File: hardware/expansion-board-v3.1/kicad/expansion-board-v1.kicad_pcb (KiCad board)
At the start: 6 copper layers, 100 x 62 mm, 156 parts, among them J1 PinHeader_2x20_P2.54mm_Vertic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, J2 U.FL_Hirose_U.FL-R-SMT-1_Vert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, J4 USB_C_Receptacle_HRO_TYPE-C-3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, J5 U.FL_Hirose_U.FL-R-SMT-1_Vert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, J6 U.FL_Hirose_U.FL-R-SMT-1_Vert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, J8 U.FL_Hirose_U.FL-R-SMT-1_Vert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, Q2 SOT-23, Q3 SOT-23, Q4 SOT-23, Q5 SOT-23, SW1 SolderJumper-2_P1.3mm_Open_Pa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, SW2 SolderJumper-2_P1.3mm_Open_Pa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, U1 SOT-23-5, U10 QFN-48-1EP_7x7mm_P0.5mm_EP5.1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, U11 DFN-8-1EP_2x2mm_P0.5mm_EP0.86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, U12 SOT-363_SC-70-6, U13 AD8319_LFCSP-8-EP, U14 MSOP-8_3x3mm_P0.65mm, U15 SOT-23-6, U16 SOT-363_SC-70-6, U17 SOT-363_SC-70-6, U2 SOT-23-5, U3 SOT-23-5, U4 BNO085_LGA-28, U5 BMP388_LGA-10, U6 LGA-16_3x3mm_P0.5mm, U7 ATGM336H_LCC-18, U8 QFN-56-1EP_7x7mm_P0.4mm_EP3.2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, U9 SOIC-8_5.3x5.3mm_P1.27mm, Y1 Crystal_SMD_3225-4Pin_3.2x2.5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, Y2 Crystal_SMD_3225-4Pin_3.2x2.5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, Y3 Crystal_SMD_3215-2Pin_3.2x1.5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

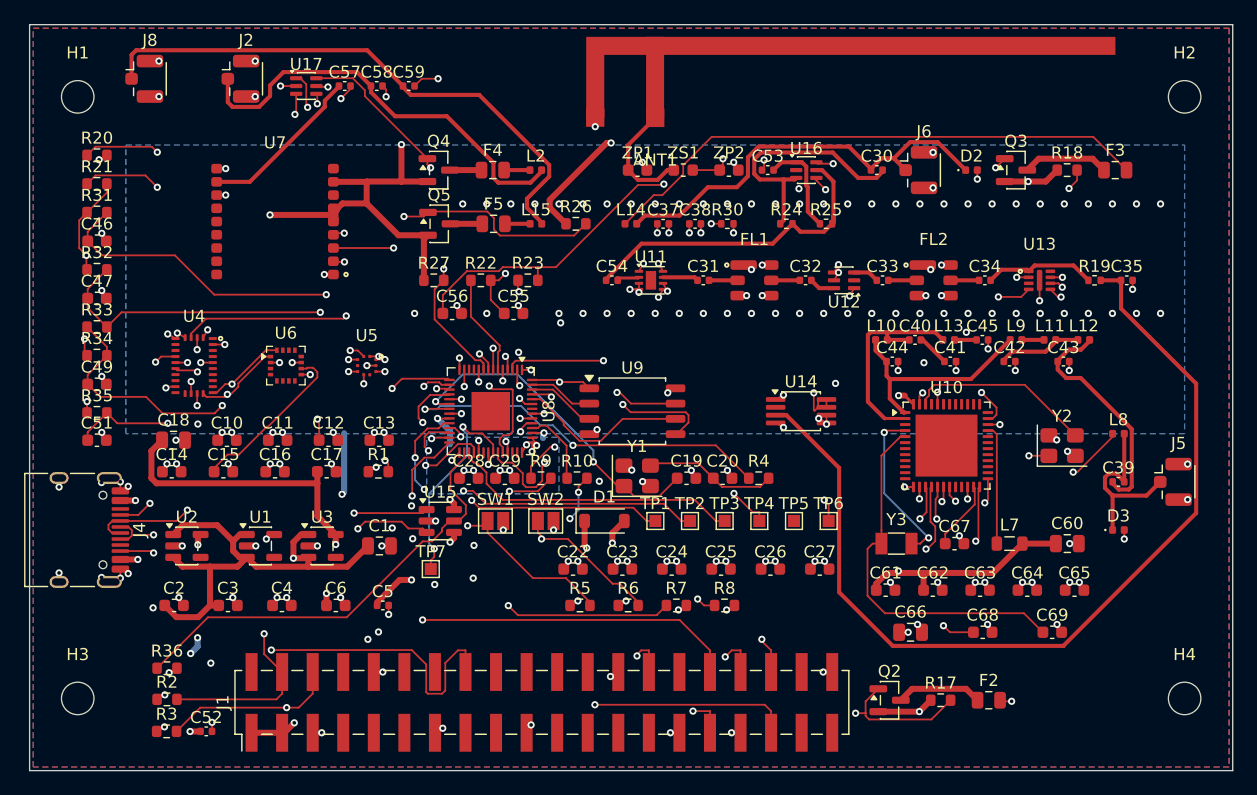
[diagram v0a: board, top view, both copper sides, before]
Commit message: feat(hw): v3.1 致命电源打通——扇出改在 route_rf 之前跑
route_rf.py 原本幂等地清掉所有 track，把 fanout_v31.py 放的扇出孔也删了。
改为只清平面网(GND/3V3_*)输出，保留信号网扇出。

新顺序：gen_pcb → fanout(空板放 9/10 孔) → route_rf(避让扇出) →
export_dsn → freerouting → import_ses。

结果：SUBG_VDDR、RP_1V1 两路致命电源打通（4层时代+上一版的死结），
板子现在能启动。铜层 DRC 0 违例。

代价：freerouting 随机性导致 RF 段 172→163（扇出挤占），5 条 RF +
USB/sub-GHz/I2C 共 15 残线待手工收尾（均非启动致命）。

下轮：RP_1V1 专用扇出（少挤 RF）+ RF 手工 F.Cu + USB/sub-GHz 手工。
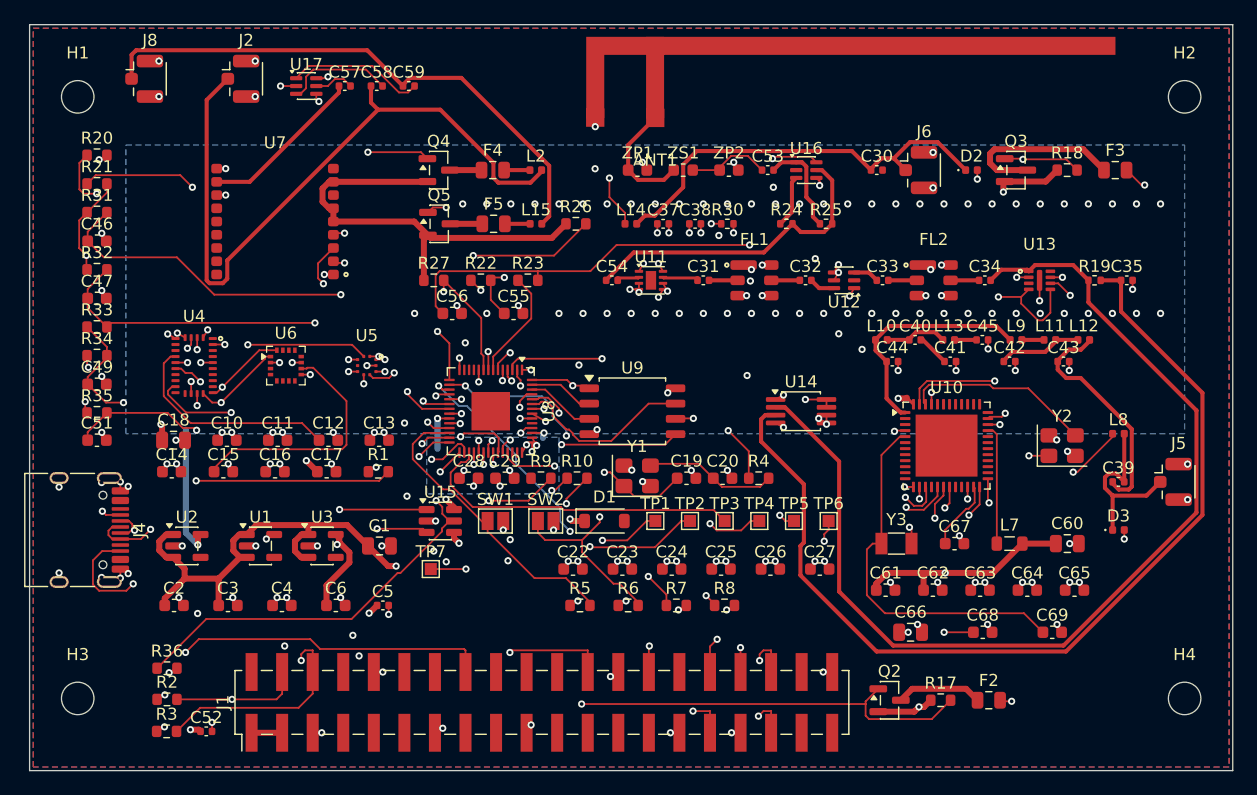
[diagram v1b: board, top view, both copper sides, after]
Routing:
- net DET_IN: track 9.26 -> 86.4 mm
- net SUBG_SCK: track 62.5 -> 0.00 mm, vias 3 -> 0
- net USB_VBUS: track 50.7 -> 0.00 mm, vias 3 -> 0
- net BARO_INT: track 0.00 -> 37.9 mm, vias 0 -> 2
- net 3V3_GNSS: track 213.3 -> 183.2 mm, vias 7 -> 6
- net DEMOD2: track 0.00 -> 28.8 mm, vias 0 -> 2
- net VCC_5V: track 85.4 -> 58.1 mm, vias 3 -> 2
- net ANT_GNSS_EXT: track 35.2 -> 58.2 mm
- net TL_PWM: track 61.8 -> 39.5 mm, vias 3 -> 2
- net SW1_J2: track 20.9 -> 4.36 mm
- net RSSI: track 63.7 -> 47.8 mm
- net SUBG_RFN: track 18.3 -> 5.20 mm
- net SUBG_TMSC: track 65.8 -> 53.2 mm, vias 3 -> 2
- net AD8313_VOUT: track 90.3 -> 78.9 mm
- net SUBG_CSN: track 59.7 -> 48.6 mm
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
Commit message: feat(hw): 收尾布线器 route_fix — 真缺线 21→10，铜层 DRC 保持 0
route_maze 布不动的真因不是复杂度，是障碍模型：它拿 track 的 bounding box
当障碍（route_maze.py:100-103），而本板 1308 段里 610 段是 45° 斜线，实测
bbox 面积 3290mm² vs 实际铜面积 778mm² —— 4.2 倍的假障碍糊满整图，A* 每次
都得翻完整个搜索空间才能报"走不通"，于是"单条几分钟"。

route_fix.py 换掉四处：
· 线段光栅化代替 bbox，代价正比线长而非包围盒面积，不再产生假障碍
· (count, owner) 双数组代替 per-net 重建占用区，查询 O(1)，一次建图全程复用
· 按网络类分档（Default 0.15/0.15、POWER 0.3/0.2、RF50 0.34/0.15）。原来
  全板按最严的 0.2 净空一刀切，比板规严得多
· 连通块解析：DRC 说的是"这两块铜没连上"，起点必须是整块铜而不是一个点

另加两个针对本板的机制：
· 焊盘逃逸 stub —— QFN 引脚该沿轴向出线，精确算 U10（0.5mm pitch）邻居边缘
  到中心线 0.375mm > 0.3 线所需的 0.35mm，是过得去的；0.15mm 栅格表达不了
  这 0.025mm 余量才误判成"几何封死"。这一段用连续几何算，绕开栅格
· 平面命中 —— In3.Cu 是 3V3_DIG 满板平面，打过孔落到填充铜上即连通，不必
  横穿半块板去够对面焊盘。判据必须是 HitTestFilledArea 而非层号，否则起点
  自己在 In3 上有段走线就会"零节点成功"

顺带修掉两个会进制造文件的真 bug：
· 过孔穿层漏检：通孔穿透全部 6 层，原先只校验起止两层，中间层直撞别人走线，
  实测放过 9 条 Via[X] on F.Cu-B.Cu <-> Track[Y] on In2/In3
· 栅格化误差：栅格只保证格点在安全圈外，45° 步长 0.212mm 的线段中点偏离
  格点 0.106mm，能蹭进净空（实测漏过 actual 0.1586 < 0.2）。现在落盘前一律
  做连续几何复核，不过就弃用该路径——宁可不布，不往板里塞违例

实测：未连通 28→17，真缺线 21→10，铜层 DRC 0→0，射频 163 段全 F.Cu、0 过孔
完全没动，整批 32 秒（原先单条几分钟）。

rip-up & reroute 也实现了（collect_blockers/strip），但结论是不该用：拆掉的线
重布不回来，迭代在 14→18→17 之间震荡且引入 20 条 clearance/shorting，已加验收
回滚。默认不启用。

⚠️ score.py 的口径偏乐观（报 3 处 vs DRC 10 处）：焊盘落在覆铜填充区就算连上，
而 KiCad 可能因 thermal spoke 不足判未连接。参考用，别当验收。

另记一条坑：check_route.py 的三分类不稳定，同一份文件跑两次会在 12/13/3 和
21/2/5 之间漂——同一个未连通对，KiCad 描述成 Pad↔X 还是 Track↔X 取决于内部
遍历顺序。验收要盯"未连通总数 + 铜层 DRC"这两个稳定量。
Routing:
- net 3V3_DIG: track 36.0 -> 68.3 mm
- net VCC_5V: track 58.1 -> 78.0 mm
- net RP_1V1: track 9.95 -> 21.3 mm, vias 5 -> 6
- net USB_VBUS: track 0.00 -> 10.5 mm, vias 0 -> 2

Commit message: fix(hw): 修掉会把短路写进板子的碰撞判定 bug；In3 锁电源平面，3V3 未连通 6→0
## 一、碰撞判定漏判交叉 —— 会真的短路，最要紧

route_fix 判两条走线冲突用的是"四端点到对方线段距离取最小"。这个公式对
**交叉**的线段返回正值：两条线真穿过彼此时，四个端点离对方线段都可能很远。

实测它布出来的 SWDIO：
    SWDIO     (104.890,91.253)→(104.890,92.353)   垂直
    SUBG_CSN  (122.332,91.980)→(103.615,91.980)   水平
    交点 (104.890,91.980) 落在两段内 —— 真短路
    公式却算出 0.3733mm、余量 +0.07mm，判为合规

seg_seg_dist 加叉积跨越判定，相交返回 0。回归：交叉→0.0，平行→1.0。
修完 route_fix 老实报"SWDIO 走不通，挡路者 SWCLK/SUBG_CSN"，不再硬布。
fanout_ring 里同样的写法一并修（它的 stub_ok 也是四端点取最小）。

KiCad DRC 本身会抓 tracks_crossing，而每次落盘都跑 DRC，所以短路没进过
制造文件——但工具带着这个 bug 就是隐患。

## 二、3V3 未连通的真因不是线宽，是叠层用途冲突

In3.Cu 既铺 3V3_DIG 电源平面（4780mm²），又被 freerouting 走了 181 段信号，
覆铜避让把平面切成 14 块孤岛，KiCad 直接报
"Zone [3V3_DIG] on In3.Cu ↔ Zone [3V3_DIG] on In3.Cu"。

· export_dsn 把 In3 加进 PLANE_LAYERS 锁死（走线层 4→3，B.Cu 原本只用了
  24 段，余量足够吸收被赶出来的 181 段）
· route_fix 的 A* 也跟着限制：平面层只对它自己的网络开放同层移动，别的网络
  只能打通孔穿过（不然 USB_VBUS 的补线又在 In3 上走了 11 段）

结果：In3 信号走线 181→0 段，平面碎块 14→1，3V3_DIG 未连通 6→0 项。

## 三、POWER 线宽拆两档（评审指出的"缩窄以适配针脚密度"）

整类 0.5mm 出不了 QFN 引脚：0.5 线从 0.25mm 宽的焊盘引出需要 0.25+0.2=0.45mm
通道，而 U8 引脚 pitch 只有 0.4mm。
· POWER（VCC_5V/USB_VBUS，USB 输入干路）保持 0.5mm
· 新增 POWER_LO 9 条低压轨 0.25mm/0.15mm。3V3_DIG≈150mA，0.25mm 1oz 载流
  约 0.9A，余量 6 倍

## 四、过孔按工厂真实能力收（已核实官网 capabilities 页）

嘉立创 6 层标准档：线宽/线距 0.09、最小 via 0.15 孔/0.25 盘、孔到孔 0.2、
via-in-pad 6 层默认标配。我们原来 0.3/0.6 比工厂下限保守一倍。
收到 0.2/0.4（环宽 0.1mm，是官方最小 0.05 的两倍），板规下限同步跟上——
不同步的话新过孔会被自己的板规判违例（实测 172+172 条）。

## 五、其它

· clean_dangling.py：只删 KiCad DRC 点名的悬空走线。route_fix clean 那种
  按连通块删碎铜在本板是负收益（未连通 16→20，还留 3 个悬空过孔），因为有些
  碎铜实际压在覆铜上是连通的
· route_fix 落盘丢弃零长度段（freerouting 的 SES 会带进 0.0001mm 残段）
· 中间产物从 /tmp 挪进工程内 build/（PK_BUILD_DIR），可随时核对、不会被系统
  清掉；大文件 .gitignore 不入库，可由 reroute.sh 完全重生成

## 验收（check_route.py exit=0，四条硬约束全过）

                  改前        改后
未连通            17          16
铜层 DRC          0           0
3V3_DIG 未连通    6 项        0 项
In3 信号走线      181 段      0 段
3V3_DIG 平面      14 块碎片   1 块完整
freerouting       25 分不收敛  5 分钟收敛 / 18 unrouted
走线分层  F952/In2:195/In3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
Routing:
- net DET_IN: track 86.4 -> 26.8 mm
- net USB_CC1: track 52.3 -> 0.00 mm, vias 2 -> 0
- net SUBG_SCK: track 0.00 -> 47.5 mm, vias 0 -> 2
- net RSSI: track 47.8 -> 2.93 mm, vias 2 -> 0
- net USB_VBUS: track 10.5 -> 55.0 mm
- net DET_INLO: track 80.7 -> 37.9 mm
- net SWDIO: track 37.1 -> 0.00 mm, vias 3 -> 0
- net 3V3_DIG: track 68.3 -> 36.7 mm, vias 44 -> 45
- net ANT_GNSS_EXT: track 58.2 -> 31.8 mm
- net GNSS_RF_IN: track 13.8 -> 0.00 mm
- net SUBG_RESET: track 62.9 -> 49.5 mm, vias 3 -> 2
- net SUBG_N3: track 4.56 -> 17.4 mm
- net SUBG_RFP: track 19.4 -> 7.22 mm
- net RP_1V1: track 21.3 -> 9.26 mm
- net SUBG_TCKC: track 62.4 -> 50.7 mm, vias 3 -> 2
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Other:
- board text added: "(c) Pilot Kit"
- board text added: "1090 / 978 ADS-B + GNSS + IMU + BARO"
- board text added: "1090 EXT"
- board text added: "1090MHz IFA ANT"
- board text added: "978 UAT"
- board text added: "GNSS EXT"
- board text added: "GNSS INT"
- board text added: "Pilot Kit Avionics Board"
- board text added: "USB"
- board text added: "V1 2026-08"
- board text added: "https://air.club"

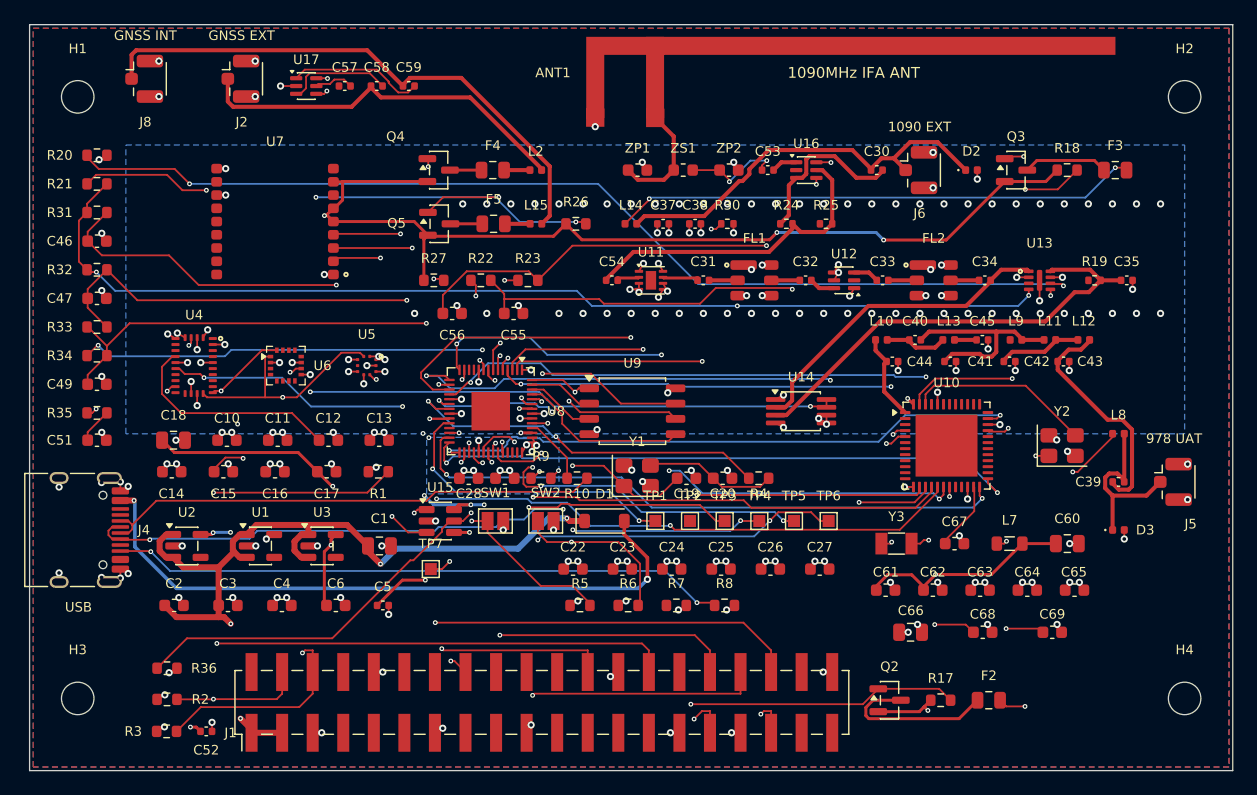
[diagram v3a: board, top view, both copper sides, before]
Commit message: fix(hw): 射频精修补两个漏判；试"射频先布"流程，结论是不如 plain（17 vs 16）
## 两个真 bug（跟流程选择无关，必须修）

1. **漏了 U.FL 自带禁布区**。route_rf_manual 自建局部占用图，只收了
   pads/trks/vias——而 snap_obstacles() 不返回 footprint 的 Zones
   （route_fix 只在建全局图时处理，见 route_fix.py:216「谁都不许走」）。
   结果射频线直接从天线口连接器身上压过去：实测 4 条 items_not_allowed +
   3 条 solder_mask_bridge，全在 J2/J6/J8 三个 U.FL 上。补上后
   ANT1090_EXT 那段从直穿 4.15mm 变成绕行 7.55mm。

2. **一条网络只布一个缺口就收工**。射频网络常有 3 块以上铜（芯片脚 + 中间
   元件 + 天线口），local_route 一次只接最近的一对。板上看着"27 条全布通"，
   实际每条都还剩缺口——实测未连通反而从 17 升到 37。改成迭代到 blocks_of
   返回单块为止，每段布完立刻挂上 board 并清 OBST 快照，否则下一轮对着同一个
   缺口反复布同一条线。

## 试了"射频先布 → keepout → freerouting"，结论：不如 plain

起因是 krt_route.sh 的注释：「射频必须先布……最后布只有 1/6 通，先布 26/27 通」，
而我的 6 条 RF 残线正好是"最后布"的症状。空板实验也支持：27 条射频在空板上
全部布通（SUBG_RFN 只要 1 段 1.25mm，在已布线板上完全无解）。

但整条流程跑完，结果是 **17 未连通 / 射频 8 条未连通**，不如 plain 的 16 / 6。
原因：27 条射频在空板上**互相抢通道**——按字母序布，先布的 ANT_* 占了后面
SW1_J*/DET_INLO 的路，换汤不换药。KRT 能到 26/27 靠的是 neck-down + 更好的
算法，我的布线器只做到 19/27 完全连通。

（KRT 本身已经找不回来了：它和它的 venv 都装在 /tmp/krt、/tmp/krtenv，
被系统清掉，仓库里没留安装来源——正好印证了产物不该放 /tmp。）

## 附三个诊断工具

- rf_diag.py    每条残线的缺口两端 + 附近挡路者余量（负值=现在就违例）
- rf_occmap.py  打印某点周围的可走图，看射频能不能出得来（PK_MAP_RAD 调范围）
- rf_flood.py   洪水填充，区分"通道太窄"和"根本被围死"。就是它定的案：
                SUBG_RFN 从 balun 端可达 y 上限 81.15 = U10 焊盘上边缘，
                目标在 82.60 够不着，封锁边界主力是 SUBG_N3 自己的走线 249 格

## 当前板子状态

未连通 17 / 铜层 DRC **0** / 射频 116 段全 F.Cu、0 过孔 / In1 参考面完整。
比 e917f2a 的 16 差 1 项。要回到 plain 版由评审定，我不擅自 git 回滚。
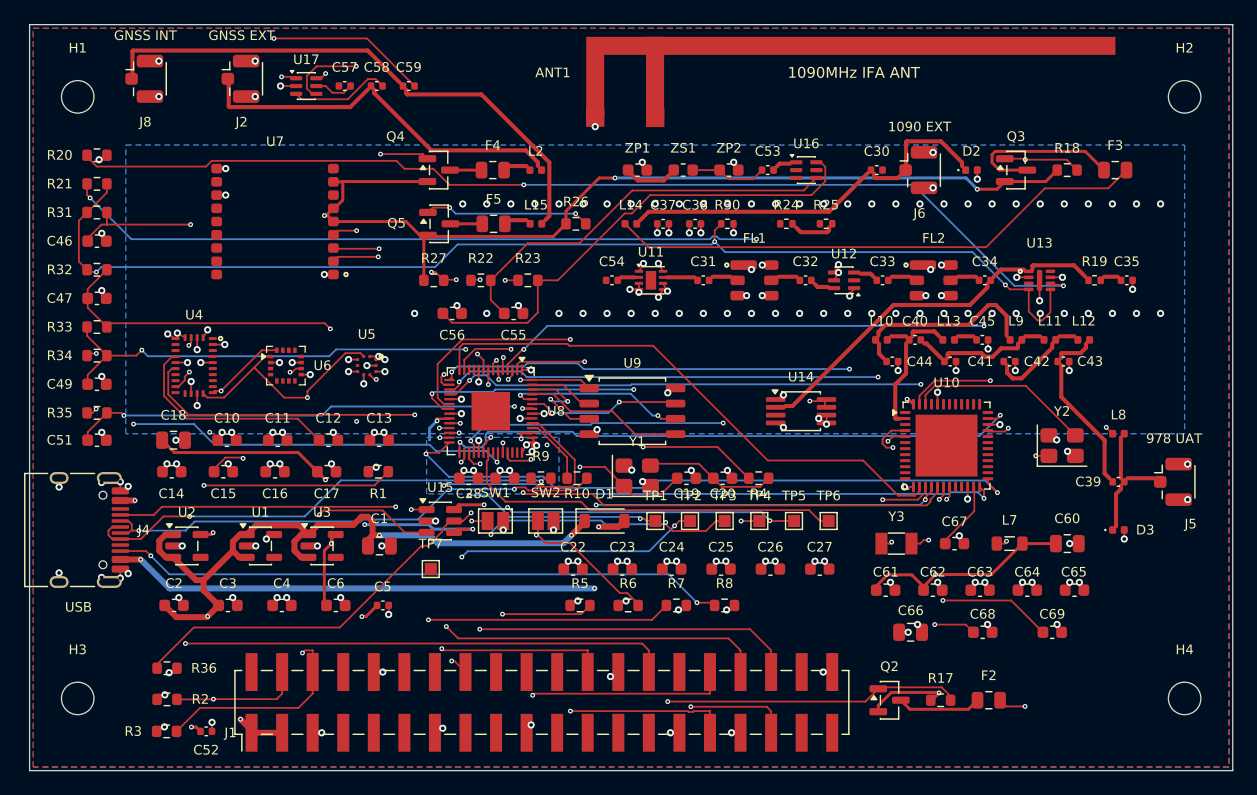
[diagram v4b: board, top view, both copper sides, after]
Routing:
- net USB_CC1: track 0.00 -> 54.0 mm, vias 0 -> 2
- net RSSI: track 2.93 -> 44.8 mm, vias 0 -> 3
- net DET_INLO: track 37.9 -> 1.15 mm
- net SWDIO: track 0.00 -> 32.9 mm, vias 0 -> 3
- net SW1_J1: track 26.9 -> 3.23 mm
- net RECOVERED_CLK: track 18.6 -> 0.00 mm, vias 2 -> 0
- net SW1_J2: track 14.1 -> 0.00 mm
- net RP_XIN: track 26.5 -> 36.5 mm, vias 3 -> 2
- net TL_PWM: track 49.9 -> 40.3 mm
- net SUBG_IRQ: track 58.8 -> 50.8 mm
- net SUBG_RFP: track 7.22 -> 15.2 mm
- net SUBG_N3: track 17.4 -> 10.1 mm
- net SLICER_LEVEL: track 51.1 -> 44.1 mm
- net RF1090_FUSE: track 7.04 -> 13.9 mm
- net SUBG_FUSE: track 13.9 -> 7.00 mm
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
